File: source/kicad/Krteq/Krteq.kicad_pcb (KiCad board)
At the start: 2 copper layers, 340.5 x 159.5 mm, 254 parts, among them Q1 Q_NMOS_GSD, SW1 Switch, SW10 Switch, SW11 Switch, SW12 Switch, SW13 Switch, SW14 Switch, SW15 Switch, SW16 Switch, SW17 Switch, SW18 Switch, SW19 Switch, SW2 Switch, SW20 Switch, SW21 Switch, SW22 Switch, SW23 Switch, SW24 Switch, SW25 Switch, SW26 Switch, SW27 Switch, SW28 Switch, SW29 Switch, SW3 Switch, SW30 Switch, SW31 Switch, SW32 Switch, SW33 Switch, SW34 Switch, SW35 Switch, SW36 Switch, SW37 Switch, SW38 Switch, SW39 Switch, SW4 Switch, SW40 Switch, SW41 Switch, SW42 Switch, SW43 Switch, SW44 Switch, SW45 Switch, SW46 Switch, SW47 Switch, SW48 Switch, SW49 Switch, SW5 Switch, SW50 Switch, SW51 Switch, SW52 Switch, SW53 Switch, SW54 Switch, SW55 Switch, SW56 Switch, SW57 Switch, SW58 Switch, SW59 Switch, SW6 Switch, SW60 Switch, SW61 Switch, SW7 Switch, SW8 Switch, SW9 Switch

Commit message: switches fix
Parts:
- moved SW1 209.5 mm to (57.1, 57.1)
- moved SW2 209.5 mm to (57.1, 76.2)
- moved SW3 209.5 mm to (57.1, 95.2)
- moved SW4 209.5 mm to (57.1, 114.3)
- moved SW5 209.5 mm to (57.1, 133.3)
- moved SW56 209.5 mm to (266.7, 57.1)
- moved SW57 209.5 mm to (266.7, 76.2)
- moved SW58 209.5 mm to (266.7, 95.2)
- moved SW59 209.5 mm to (266.7, 114.3)
- moved SW6 209.5 mm to (57.1, 152.4)
- moved SW60 209.5 mm to (266.7, 133.3)
- moved SW61 209.5 mm to (266.7, 152.4)
- moved SW10 171.4 mm to (76.2, 133.3)
- moved SW11 171.4 mm to (76.2, 152.4)
- moved SW51 171.4 mm to (247.7, 76.2)
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
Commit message: case updates
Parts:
- D1, D2, D3: footprint LED_THT:LED_D3.0mm -> LED_THT:LED_D5.0mm
- SW1, SW10, SW11, SW12, SW13, SW14, SW15, SW16, SW17, SW18, SW19, SW2, SW20, SW21, SW22, SW23, SW24, SW25, SW26, SW27, SW28, SW29, SW3, SW30, SW32, SW33, SW34, SW35, SW36, SW37, SW38, SW39, SW4, SW40, SW41, SW42, SW43, SW44, SW45, SW46, SW47, SW48, SW49, SW5, SW50, SW51, SW52, SW53, SW54, SW55, SW56, SW57, SW58, SW59, SW6, SW60, SW61, SW7, SW8, SW9: value Switch -> Switch 1u
- SW31: value Switch -> Switch 2u
- moved D1 2.38 mm to (148.8, 52.4)
- moved D3 2.38 mm to (172.6, 52.4)
- moved R3 2.38 mm to (178.9, 63.1)
- moved R1 1.19 mm to (155.1, 63.1)

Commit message: case update
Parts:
- Q1, R65, R66: moved to B.Cu
- moved R66 61.7 mm to (73.8, 63.1), turned to 180 degrees
- moved Q1 57.1 mm to (73.5, 58.0), turned to 180 degrees
- moved R65 52.2 mm to (73.6, 53.3), turned to 180 degrees
- moved A1 15.0 mm to (132.2, 67.7)
- moved R1 10.8 mm to (156.0, 52.4), turned to -90 degrees
- moved R3 10.8 mm to (179.8, 52.4), turned to -90 degrees
- moved R2 6.02 mm to (167.9, 52.4), turned to -90 degrees
- moved D1 3.00 mm to (148.8, 55.4)
- moved D2 3.00 mm to (160.7, 55.4)
- moved D3 3.00 mm to (172.6, 55.4)

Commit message: pcb placement
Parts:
- removed R10, R11, R12, R13, R14, R15, R16, R17, R18, R19, R20, R21, R22, R23, R24, R25, R26, R27, R28, R29, R30, R31, R32, R33, R34, R35, R36, R37, R38, R39, R40, R41, R42, R43, R44, R45, R46, R47, R48, R49, R50, R51, R52, R53, R54, R55, R56, R57, R58, R59, R6, R60, R61, R62, R63, R64, R7, R8, R9: 330, Resistor_SMD:R_0603_1608Metric
- added R100: 330, Resistor_SMD:R_0603_1608Metric, B.Cu at (242.9, 100.3)
- added R101: 330, Resistor_SMD:R_0603_1608Metric, B.Cu at (242.9, 119.4)
- added R102: 330, Resistor_SMD:R_0603_1608Metric, B.Cu at (242.9, 138.4)
- added R103: 330, Resistor_SMD:R_0603_1608Metric, B.Cu at (242.9, 157.5)
- added R104: 330, Resistor_SMD:R_0603_1608Metric, B.Cu at (242.9, 176.5)
- added R105: 330, Resistor_SMD:R_0603_1608Metric, B.Cu at (261.9, 100.3)
- added R106: 330, Resistor_SMD:R_0603_1608Metric, B.Cu at (261.9, 119.4)
- added R107: 330, Resistor_SMD:R_0603_1608Metric, B.Cu at (261.9, 138.4)
- added R108: 330, Resistor_SMD:R_0603_1608Metric, B.Cu at (261.9, 157.5)
- added R109: 330, Resistor_SMD:R_0603_1608Metric, B.Cu at (261.9, 176.5)
- added R110: 330, Resistor_SMD:R_0603_1608Metric, B.Cu at (281.0, 100.3)
- added R111: 330, Resistor_SMD:R_0603_1608Metric, B.Cu at (281.0, 119.4)
- added R112: 330, Resistor_SMD:R_0603_1608Metric, B.Cu at (281.0, 138.4)
- added R113: 330, Resistor_SMD:R_0603_1608Metric, B.Cu at (281.0, 157.5)
- added R114: 330, Resistor_SMD:R_0603_1608Metric, B.Cu at (281.0, 176.5)
- added R115: 330, Resistor_SMD:R_0603_1608Metric, B.Cu at (300.0, 100.3)
- added R116: 330, Resistor_SMD:R_0603_1608Metric, B.Cu at (300.0, 119.4)
- added R117: 330, Resistor_SMD:R_0603_1608Metric, B.Cu at (300.0, 138.4)
- added R118: 330, Resistor_SMD:R_0603_1608Metric, B.Cu at (300.0, 157.5)
- added R119: 330, Resistor_SMD:R_0603_1608Metric, B.Cu at (300.0, 176.5)
- added R120: 330, Resistor_SMD:R_0603_1608Metric, B.Cu at (319.1, 81.3)
- added R121: 330, Resistor_SMD:R_0603_1608Metric, B.Cu at (319.1, 100.3)
- added R122: 330, Resistor_SMD:R_0603_1608Metric, B.Cu at (319.1, 119.4)
- added R123: 330, Resistor_SMD:R_0603_1608Metric, B.Cu at (319.1, 138.4)
- added R124: 330, Resistor_SMD:R_0603_1608Metric, B.Cu at (319.1, 157.5)
- added R125: 330, Resistor_SMD:R_0603_1608Metric, B.Cu at (319.1, 176.5)
- added R67: 330, Resistor_SMD:R_0603_1608Metric, B.Cu at (109.5, 119.4)
- added R68: 330, Resistor_SMD:R_0603_1608Metric, B.Cu at (109.5, 138.4)
- added R69: 330, Resistor_SMD:R_0603_1608Metric, B.Cu at (109.5, 157.5)
- added R70: 330, Resistor_SMD:R_0603_1608Metric, B.Cu at (109.5, 176.5)
- added R71: 330, Resistor_SMD:R_0603_1608Metric, B.Cu at (128.6, 100.3)
- added R72: 330, Resistor_SMD:R_0603_1608Metric, B.Cu at (128.6, 119.4)
- added R73: 330, Resistor_SMD:R_0603_1608Metric, B.Cu at (128.6, 138.4)
- added R74: 330, Resistor_SMD:R_0603_1608Metric, B.Cu at (128.6, 157.5)
- added R75: 330, Resistor_SMD:R_0603_1608Metric, B.Cu at (128.6, 176.5)
- added R76: 330, Resistor_SMD:R_0603_1608Metric, B.Cu at (147.6, 100.3)
- added R77: 330, Resistor_SMD:R_0603_1608Metric, B.Cu at (147.6, 119.4)
- added R78: 330, Resistor_SMD:R_0603_1608Metric, B.Cu at (147.6, 138.4)
- added R79: 330, Resistor_SMD:R_0603_1608Metric, B.Cu at (147.6, 157.5)
- added R80: 330, Resistor_SMD:R_0603_1608Metric, B.Cu at (147.6, 176.5)
- added R81: 330, Resistor_SMD:R_0603_1608Metric, B.Cu at (166.7, 100.3)
- added R82: 330, Resistor_SMD:R_0603_1608Metric, B.Cu at (166.7, 119.4)
- added R83: 330, Resistor_SMD:R_0603_1608Metric, B.Cu at (166.7, 138.4)
- added R84: 330, Resistor_SMD:R_0603_1608Metric, B.Cu at (166.7, 157.5)
- added R85: 330, Resistor_SMD:R_0603_1608Metric, B.Cu at (166.7, 176.5)
- added R86: 330, Resistor_SMD:R_0603_1608Metric, B.Cu at (185.7, 100.3)
- added R87: 330, Resistor_SMD:R_0603_1608Metric, B.Cu at (185.7, 119.4)
- added R88: 330, Resistor_SMD:R_0603_1608Metric, B.Cu at (185.7, 138.4)
- added R89: 330, Resistor_SMD:R_0603_1608Metric, B.Cu at (185.7, 157.5)
- added R90: 330, Resistor_SMD:R_0603_1608Metric, B.Cu at (185.7, 176.5)
- added R91: 330, Resistor_SMD:R_0603_1608Metric, B.Cu at (204.8, 100.3)
- added R92: 330, Resistor_SMD:R_0603_1608Metric, B.Cu at (204.8, 119.4)
- added R93: 330, Resistor_SMD:R_0603_1608Metric, B.Cu at (204.8, 138.4)
- added R94: 330, Resistor_SMD:R_0603_1608Metric, B.Cu at (204.8, 157.5)
- added R95: 330, Resistor_SMD:R_0603_1608Metric, B.Cu at (214.3, 176.5)
- added R96: 330, Resistor_SMD:R_0603_1608Metric, B.Cu at (223.8, 100.3)
- added R97: 330, Resistor_SMD:R_0603_1608Metric, B.Cu at (223.8, 119.4)
- added R98: 330, Resistor_SMD:R_0603_1608Metric, B.Cu at (223.8, 138.4)
- added R99: 330, Resistor_SMD:R_0603_1608Metric, B.Cu at (223.8, 157.5)
- D10, D100, D101, D102, D103, D104, D105, D106, D107, D108, D109, D11, D110, D111, D112, D113, D114, D115, D116, D117, D118, D119, D12, D120, D121, D122, D123, D124, D125, D13, D14, D15, D16, D17, D18, D19, D20, D21, D22, D23, D24, D25, D26, D27, D28, D29, D30, D31, D32, D33, D34, D35, D36, D37, D38, D39, D4, D40, D41, D42, D43, D44, D45, D46, D47, D48, D49, D5, D50, D51, D52, D53, D54, D55, D56, D57, D58, D59, D6, D60, D61, D62, D63, D64, D65, D66, D67, D68, D69, D7, D70, D71, D72, D73, D74, D75, D76, D77, D78, D79, D8, D80, D81, D82, D83, D84, D85, D86, D87, D88, D89, D9, D90, D91, D92, D93, D94, D95, D96, D97, D98, D99: moved to B.Cu
- R4: value 330 -> 470; moved to B.Cu
- R5: value 330 -> 10k; moved to B.Cu
- R65: value 470 -> 330
- R66: value 10k -> 330
- moved D9 239.8 mm to (120.2, 176.5)
- moved D14 235.3 mm to (139.3, 176.5)
- moved D8 232.8 mm to (120.2, 157.5)
- moved D70 231.2 mm to (114.3, 176.5)
- moved D13 227.1 mm to (139.3, 157.5)
- moved D7 226.5 mm to (120.2, 138.4)
- moved D69 226.4 mm to (114.3, 157.5)
- moved D75 225.0 mm to (133.4, 176.5)
- moved R4 223.0 mm to (136.7, 80.4)
- moved R5 222.9 mm to (136.7, 83.4)
- moved D68 222.5 mm to (114.3, 138.4)
- moved D6 221.3 mm to (120.2, 119.4)
- moved D67 219.5 mm to (114.3, 119.4)
- moved D74 219.0 mm to (133.3, 157.5)
- moved D66 217.6 mm to (114.3, 100.3)
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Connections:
- A1 pad 21: ROW4 -> BL PWM
- A1 pad 22: ROW5 -> unconnected-(A1-GPIO17-Pad22)
- A1 pad 24: SIG1 -> ROW4
- A1 pad 25: SIG2 -> ROW5
- A1 pad 26: SIG3 -> SIG1
- A1 pad 27: BL PWM -> SIG2
- A1 pad 29: unconnected-(A1-GPIO22-Pad29) -> SIG3
- R4 pad 1: Net-(D65-K) -> Net-(Q1-G)
- R4 pad 2: BL DRAIN -> BL PWM
- R5 pad 1: Net-(D66-K) -> Net-(Q1-G)
- R5 pad 2: BL DRAIN -> GND
- R65 pad 1: Net-(Q1-G) -> Net-(D65-K)
- R65 pad 2: BL PWM -> BL DRAIN
- R66 pad 1: Net-(Q1-G) -> Net-(D66-K)
- R66 pad 2: GND -> BL DRAIN
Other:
- board size 340.5 x 159.5 mm -> 228.6 x 116.3 mm

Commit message: 3d models
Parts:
- moved Q1 1.32 mm to (131.2, 82.4)
- moved R4 1.32 mm to (135.5, 80.9)
- moved R5 1.32 mm to (135.5, 83.9)
- moved D120 0.89 mm to (322.9, 81.3)
- moved D121 0.89 mm to (322.9, 100.3)
- moved D122 0.89 mm to (322.9, 119.4)
- moved D123 0.89 mm to (322.9, 138.4)
- moved D124 0.89 mm to (322.9, 157.5)
- moved D125 0.89 mm to (322.9, 176.5)
- moved D59 0.89 mm to (328.9, 81.3)
- moved D60 0.89 mm to (328.9, 100.3)
- moved D61 0.89 mm to (328.9, 119.4)
- moved D62 0.89 mm to (328.9, 138.4)
- moved D63 0.89 mm to (328.9, 157.5)
- moved D64 0.89 mm to (328.9, 176.5)
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
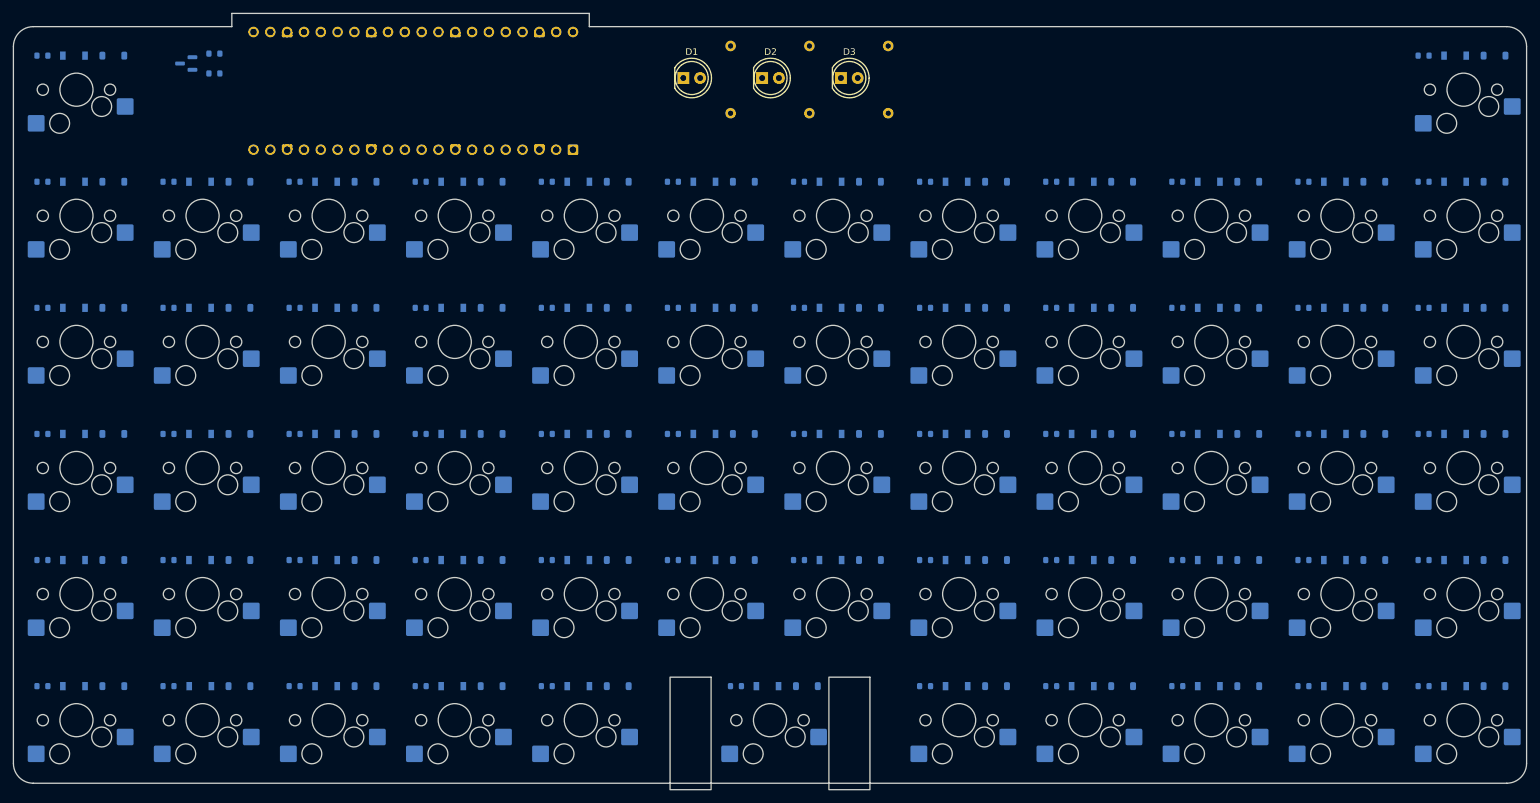
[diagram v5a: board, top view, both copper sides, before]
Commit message: extend top by 2mm
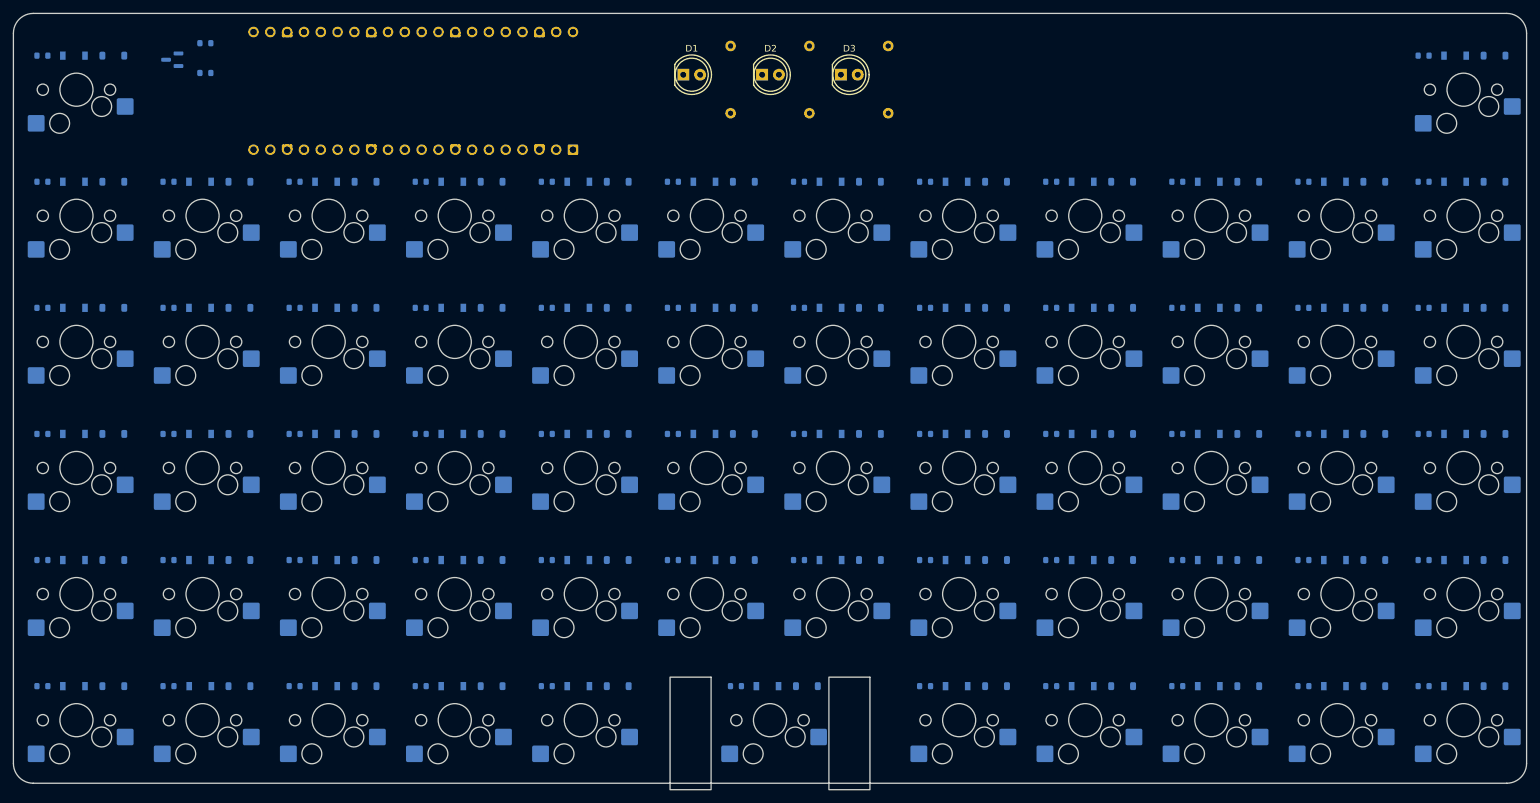
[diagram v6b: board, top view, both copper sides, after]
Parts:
- moved Q1 2.19 mm to (129.1, 81.9)
- moved R4 2.08 mm to (134.1, 79.4)
- moved R5 1.36 mm to (134.1, 83.9)
- moved D1 0.50 mm to (206.3, 84.1)
- moved D2 0.50 mm to (218.2, 84.1)
- moved D3 0.50 mm to (230.1, 84.1)
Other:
- outline, holes or cut-outs redrawn
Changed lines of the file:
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@@
 		(allow_soldermask_bridges_in_footprints no)
 		(tenting front back)
-		(grid_origin 322.925776 176.506248)
+		(grid_origin 108.125 74.875)
 		(pcbplotparams
 			(layerselection 0x00000000_00000000_55555555_5755f5ff)
@@
 	(footprint "LED_THT:LED_D5.0mm"
 		(layer "F.Cu")
-		(at 230.140625 84.6375)
+		(at 230.140625 84.1375)
 		(descr "LED, diameter 5.0mm, 2 pins, http://cdn-reichelt.de/documents/datenblatt/A500/LL-504BC2E-009.pdf, generated by kicad-footprint-generator")
 		(tags "LED")
@@
 	(footprint "LED_THT:LED_D5.0mm"
 		(layer "F.Cu")
-		(at 218.234375 84.6375)
+		(at 218.234375 84.1375)
 		(descr "LED, diameter 5.0mm, 2 pins, http://cdn-reichelt.de/documents/datenblatt/A500/LL-504BC2E-009.pdf, generated by kicad-footprint-generator")
 		(tags "LED")
@@
 	(footprint "LED_THT:LED_D5.0mm"
 		(layer "F.Cu")
-		(at 206.328125 84.6375)
+		(at 206.328125 84.1375)
 		(descr "LED, diameter 5.0mm, 2 pins, http://cdn-reichelt.de/documents/datenblatt/A500/LL-504BC2E-009.pdf, generated by kicad-footprint-generator")
 		(tags "LED")
@@
 	(footprint "Resistor_SMD:R_0603_1608Metric"
 		(layer "B.Cu")
-		(at 135.485151 83.946873)
+		(at 134.125 83.875)
 		(descr "Resistor SMD 0603 (1608 Metric), square (rectangular) end terminal, IPC-7351 nominal, (Body size source: IPC-SM-782 page 72, https://www.pcb-3d.com/wordpress/wp-content/uploads/ipc-sm-782a_amendment_1_and_2.pdf), generated with kicad-footprint-generator")
 		(tags "resistor")
@@
 	(footprint "Resistor_SMD:R_0603_1608Metric"
 		(layer "B.Cu")
-		(at 135.485151 80.946873)
+		(at 134.125 79.375)
 		(descr "Resistor SMD 0603 (1608 Metric), square (rectangular) end terminal, IPC-7351 nominal, (Body size source: IPC-SM-782 page 72, https://www.pcb-3d.com/wordpress/wp-content/uploads/ipc-sm-782a_amendment_1_and_2.pdf), generated with kicad-footprint-generator")
 		(tags "resistor")
@@
 	(footprint "Package_TO_SOT_SMD:SOT-23"
 		(layer "B.Cu")
-		(at 131.235151 82.446873 180)
+		(at 129.125 81.875 180)
 		(descr "SOT, 3 Pin (JEDEC TO-236 Var AB https://www.jedec.org/document_search?search_api_views_fulltext=TO-236), generated with kicad-footprint-generator ipc_gullwing_generator.py")
 		(tags "SOT TO_SOT_SMD")
@@
 	)
 	(gr_arc
-		(start 105.125 79.875)
-		(mid 106.00368 77.75368)
-		(end 108.125 76.875)
+		(start 105.125 77.875)
+		(mid 106.00368 75.75368)
+		(end 108.125 74.875)
 		(stroke
 			(width 0.05)
@@
 	)
 	(gr_line
-		(start 333.725 79.875)
+		(start 333.725 77.875)
 		(end 333.725 188.175)
 		(stroke
@@
 	)
 	(gr_line
-		(start 108.125 76.875)
-		(end 138.125 76.875)
+		(start 108.125 74.875)
+		(end 330.725 74.875)
 		(stroke
 			(width 0.05)
@@
 	(gr_line
 		(start 105.125 188.175)
-		(end 105.125 79.875)
+		(end 105.125 77.875)
 		(stroke
 			(width 0.05)
@@
 		(layer "Edge.Cuts")
 	)
-	(gr_line
-		(start 192.125 76.875)
-		(end 192.125 74.875)
-		(stroke
-			(width 0.05)
-			(type default)
-		)
-		(layer "Edge.Cuts")
-	)
 	(gr_arc
-		(start 330.725 76.875)
-		(mid 332.84632 77.75368)
-		(end 333.725 79.875)
+		(start 330.725 74.875)
+		(mid 332.84632 75.75368)
+		(end 333.725 77.875)
 		(stroke
 			(width 0.05)
@@
 	)
 	(gr_line
-		(start 138.125 74.875)
-		(end 138.125 76.875)
-		(stroke
-			(width 0.05)
-			(type default)
-		)
-		(layer "Edge.Cuts")
-	)
-	(gr_line
-		(start 192.125 74.875)
-		(end 138.125 74.875)
-		(stroke
-			(width 0.05)
-			(type default)
-		)
-		(layer "Edge.Cuts")
-	)
-	(gr_line
-		(start 192.125 76.875)
-		(end 330.725 76.875)
-		(stroke
-			(width 0.05)
-			(type default)
-		)
-		(layer "Edge.Cuts")
-	)
-	(gr_line
 		(start 297.125 189.175)
 		(end 314.175 189.175)
@@
 	)
 	(gr_line
-		(start 331.725 78.875)
-		(end 314.725 78.875)
-		(stroke
-			(width 0.1)
-			(type default)
-		)
-		(layer "User.4")
-	)
-	(gr_line
 		(start 276.075 171.125)
 		(end 276.075 135.125)
@@
 	(gr_line
 		(start 331.725 133.025)
-		(end 331.725 78.875)
+		(end 331.725 76.875)
 		(stroke
 			(width 0.1)
@@
 	)
 	(gr_line
-		(start 107.125 78.875)
-		(end 124.175 78.875)
-		(stroke
-			(width 0.1)
-			(type default)
-		)
-		(layer "User.4")
-	)
-	(gr_line
 		(start 276.075 173.175)
 		(end 259.025 173.175)
@@
 	(gr_line
 		(start 107.125 133.025)
-		(end 107.125 78.875)
+		(end 107.125 76.875)
 		(stroke
 			(width 0.1)

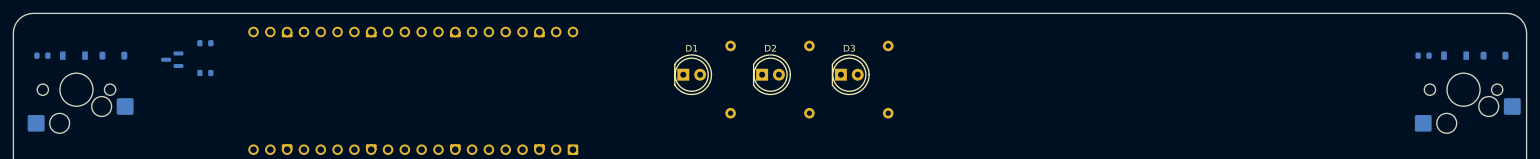
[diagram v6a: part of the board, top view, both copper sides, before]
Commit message: new LED design
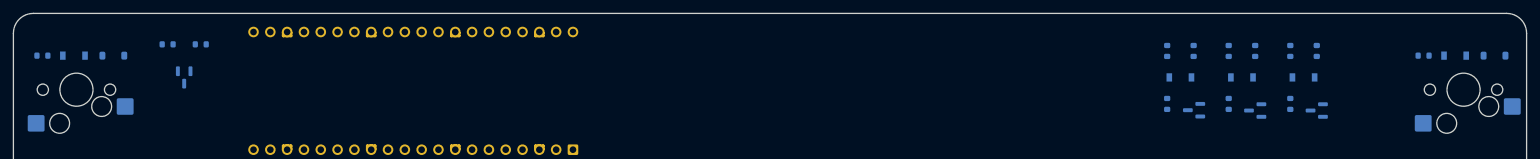
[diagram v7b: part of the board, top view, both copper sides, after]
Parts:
- added Q2: Q_NMOS_GSD, Package_TO_SOT_SMD:SOT-23, B.Cu at (292.7, 89.5)
- added Q3: Q_NMOS_GSD, Package_TO_SOT_SMD:SOT-23, B.Cu at (283.5, 89.5)
- added Q4: Q_NMOS_GSD, Package_TO_SOT_SMD:SOT-23, B.Cu at (130.9, 84.5)
- added R10: 470, Resistor_SMD:R_0603_1608Metric, B.Cu at (133.4, 79.5)
- added R11: 10k, Resistor_SMD:R_0603_1608Metric, B.Cu at (128.4, 79.5)
- added R6: 100k, Resistor_SMD:R_0603_1608Metric, B.Cu at (292.7, 80.5)
- added R7: 100, Resistor_SMD:R_0603_1608Metric, B.Cu at (279.4, 88.5)
- added R8: 100, Resistor_SMD:R_0603_1608Metric, B.Cu at (279.4, 80.5)
- added R9: 100k, Resistor_SMD:R_0603_1608Metric, B.Cu at (283.4, 80.5)
- D1, D2, D3: value THT LED -> SMD LED; footprint LED_THT:LED_D5.0mm -> Krteq:MHT151WDT; moved to B.Cu
- R1, R2: value R -> 100; footprint Resistor_THT:R_Axial_DIN0207_L6.3mm_D2.5mm_P10.16mm_Horizontal -> Resistor_SMD:R_0603_1608Metric
- R3: value R -> 100k; footprint Resistor_THT:R_Axial_DIN0207_L6.3mm_D2.5mm_P10.16mm_Horizontal -> Resistor_SMD:R_0603_1608Metric
- R4: value 470 -> 100
- R5: value 10k -> 100
- moved Q1 173.1 mm to (302.0, 89.5)
- moved R4 154.9 mm to (288.7, 88.5), turned to -90 degrees
- moved R5 154.6 mm to (288.7, 80.5), turned to 90 degrees
- moved D1 93.7 mm to (300.0, 84.5)
- moved R1 84.6 mm to (298.0, 88.5), turned to -90 degrees
- moved R2 73.3 mm to (298.0, 80.5)
- moved D2 72.5 mm to (290.7, 84.5)
- moved R3 65.4 mm to (302.0, 80.5)
- moved D3 51.3 mm to (281.4, 84.5)
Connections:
- A1 pad 26: SIG1 -> SIG3
- A1 pad 29: SIG3 -> SIG1
- A1 pad 36: 3V3 -> unconnected-(A1-3V3-Pad36)
- D1 pad 1: SIG1 -> Net-(D1-K)
- D1 pad 2: Net-(D1-A) -> VBUS
- D2 pad 1: SIG2 -> Net-(D2-K)
- D2 pad 2: Net-(D2-A) -> VBUS
- D3 pad 1: SIG3 -> Net-(D3-K)
- D3 pad 2: Net-(D3-A) -> VBUS
- Q1 pad 3: BL DRAIN -> Net-(Q1-D)
- R1 pad 1: Net-(D1-A) -> Net-(D1-K)
- R1 pad 2: 3V3 -> Net-(Q1-D)
- R2 pad 1: Net-(D2-A) -> Net-(Q1-G)
- R2 pad 2: 3V3 -> SIG1
- R3 pad 1: Net-(D3-A) -> Net-(Q1-G)
- R3 pad 2: 3V3 -> GND
- R4 pad 1: Net-(Q1-G) -> Net-(D2-K)
- R4 pad 2: BL PWM -> Net-(Q2-D)
- R5 pad 1: Net-(Q1-G) -> Net-(Q2-G)
- R5 pad 2: GND -> SIG2

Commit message: Part consolidation
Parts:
- D1, D100, D101, D102, D103, D104, D105, D106, D107, D108, D109, D110, D111, D112, D113, D114, D115, D116, D117, D118, D119, D120, D121, D122, D123, D124, D125, D2, D3, D65, D66, D67, D68, D69, D70, D71, D72, D73, D74, D75, D76, D77, D78, D79, D80, D81, D82, D83, D84, D85, D86, D87, D88, D89, D90, D91, D92, D93, D94, D95, D96, D97, D98, D99: value SMD LED -> LED
- D10, D11, D12, D13, D14, D15, D16, D17, D18, D19, D20, D21, D22, D23, D24, D25, D26, D27, D28, D29, D30, D31, D32, D33, D34, D35, D36, D37, D38, D39, D4, D40, D41, D42, D43, D44, D45, D46, D47, D48, D49, D5, D50, D51, D52, D53, D54, D55, D56, D57, D58, D59, D6, D60, D61, D62, D63, D64, D7, D8, D9: value D -> Diode
- R1, R4, R7: value 100 -> 82
- R2, R5, R8: value 100 -> 470
- R3, R6, R9: value 100k -> 10k
- SW1, SW10, SW11, SW12, SW13, SW14, SW15, SW16, SW17, SW18, SW19, SW2, SW20, SW21, SW22, SW23, SW24, SW25, SW26, SW27, SW28, SW29, SW3, SW30, SW32, SW33, SW34, SW35, SW36, SW37, SW38, SW39, SW4, SW40, SW41, SW42, SW43, SW44, SW45, SW46, SW47, SW48, SW49, SW5, SW50, SW51, SW52, SW53, SW54, SW55, SW56, SW57, SW58, SW59, SW6, SW60, SW61, SW7, SW8, SW9: value Switch 1u -> Switch
- SW31: value Switch 2u -> Switch
